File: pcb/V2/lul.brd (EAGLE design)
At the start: 90 x 96 mm, 85 parts, among them IC1 STM32F072C8T6, IC2 REG1117, IC3 74AHCT1G08DBV, SW1 324_SW324_SWITCH_FOOT_HOLE, SW10 KAILH_SWITCH_SOCKET, SW11 KAILH_SWITCH_SOCKET, SW12 KAILH_SWITCH_SOCKET, SW13 KAILH_SWITCH_SOCKET, SW14 KAILH_SWITCH_SOCKET, SW15 KAILH_SWITCH_SOCKET, SW16 KAILH_SWITCH_SOCKET, SW17 KAILH_SWITCH_SOCKET, SW18 KAILH_SWITCH_SOCKET, SW19 KAILH_SWITCH_SOCKET, SW2 324_SW324_SWITCH_FOOT_HOLE, SW3 324_SW324_SWITCH_FOOT_HOLE, SW4 324_SW324_SWITCH_FOOT_HOLE, SW5 KAILH_SWITCH_SOCKET, SW6 KAILH_SWITCH_SOCKET, SW7 KAILH_SWITCH_SOCKET, SW8 KAILH_SWITCH_SOCKET, SW9 KAILH_SWITCH_SOCKET, U1 UG-2864HSWEG01, U2 USBC_16P

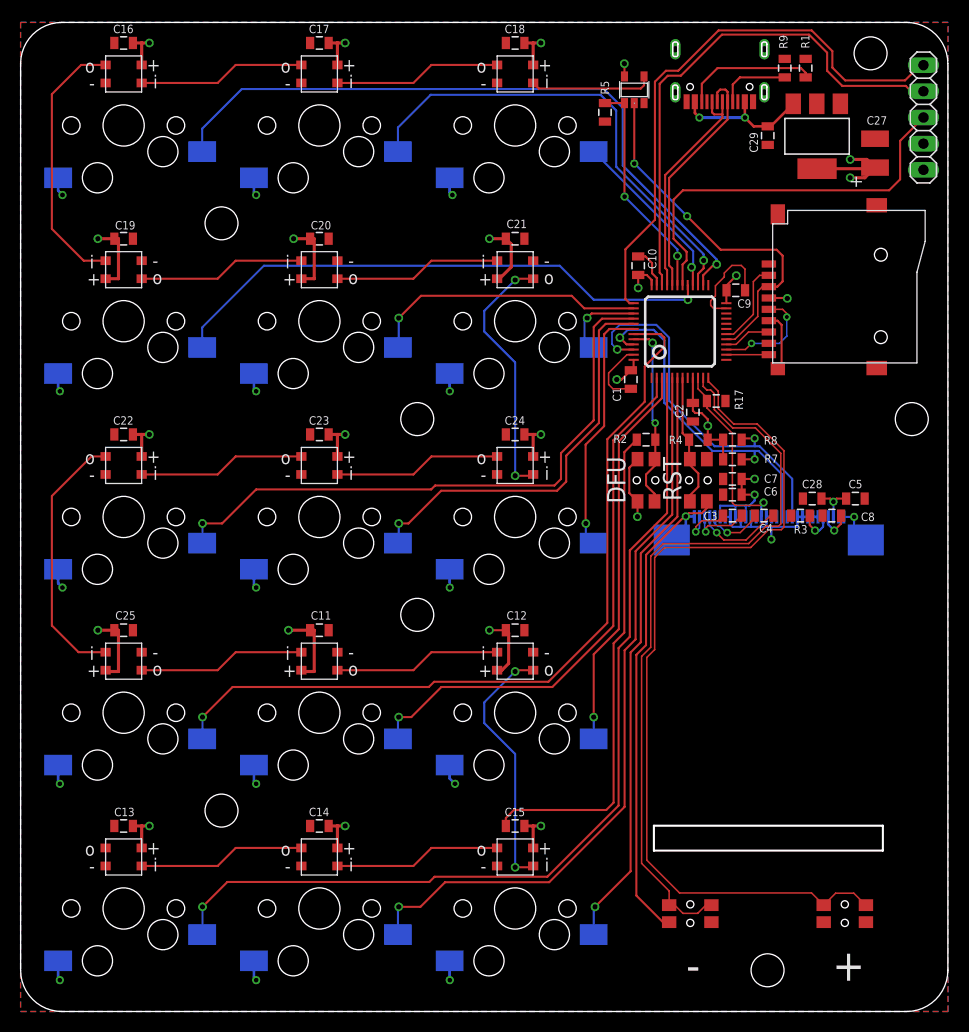
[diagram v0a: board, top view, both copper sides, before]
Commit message: added hot-swap sockets
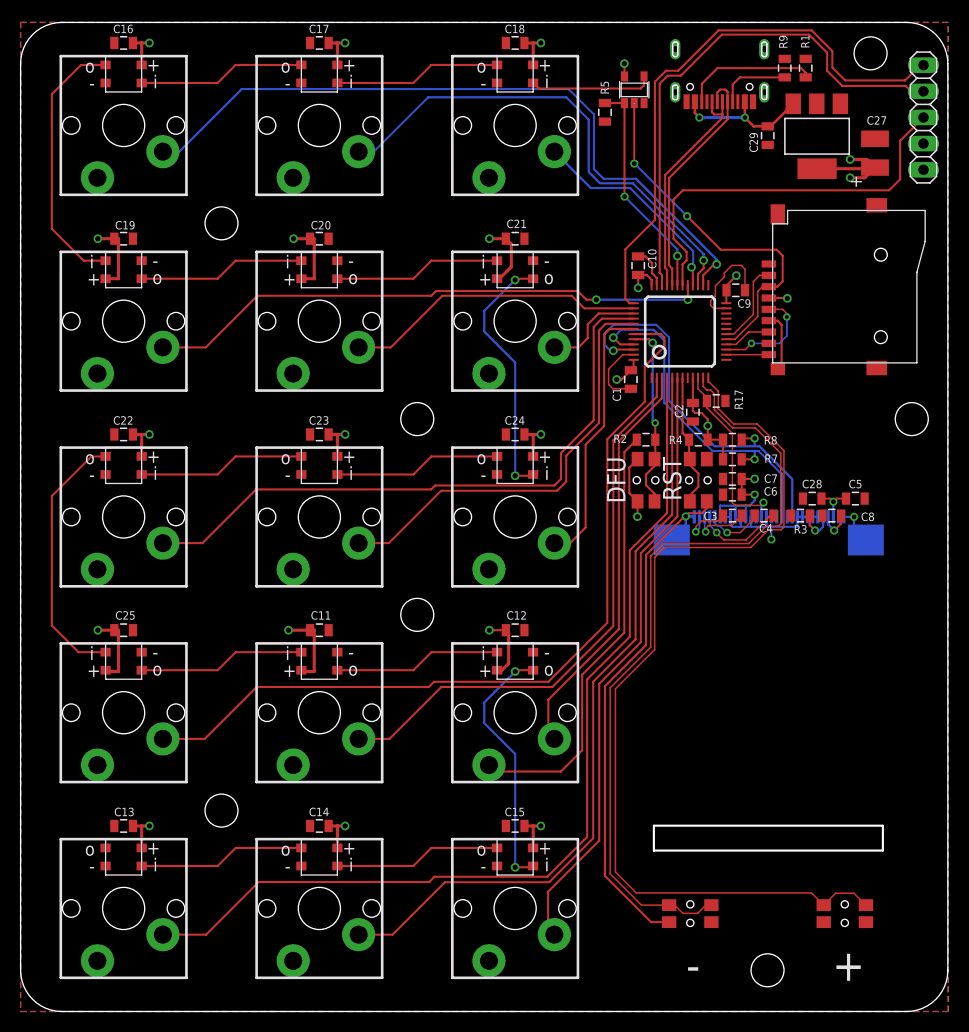
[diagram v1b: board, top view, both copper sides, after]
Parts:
- removed SW10, SW11, SW12, SW13, SW14, SW15, SW16, SW17, SW18, SW19, SW5, SW6, SW7, SW8, SW9: KAILH_SWITCH_SOCKET, Kailh_switch_socket:SWITCH_SOCKET
- added S1, S10, S11, S12, S13, S14, S15, S2, S3, S4, S5, S6, S7, S8, S9: CHERRY-MX-LED, SparkFun-Cherry-MX-Switch-Breakout:CHERRY-MX-LED
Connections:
- net GND: now also S1.S2, S10.S2, S11.S2, S12.S2, S13.S2, S14.S2, S15.S2, S2.S2, S3.S2, S4.S2, S5.S2, S6.S2, S7.S2, S8.S2, S9.S2; no longer SW10.1, SW11.1, SW12.1, SW13.1, SW14.1, SW15.1, SW16.1, SW17.1, SW18.1, SW19.1, SW5.1, SW6.1, SW7.1, SW8.1, SW9.1
- net SW1: now also S1.S1; no longer SW5.2
- net SW10: now also S10.S1; no longer SW14.2
- net SW11: now also S11.S1; no longer SW15.2
- net SW12: now also S12.S1; no longer SW16.2
- net SW13: now also S13.S1; no longer SW17.2
- net SW14: now also S14.S1; no longer SW18.2
- net SW15: now also S15.S1; no longer SW19.2
- net SW2: now also S2.S1; no longer SW6.2
- net SW3: now also S3.S1; no longer SW7.2
- net SW4: now also S4.S1; no longer SW8.2
- net SW5: now also S5.S1; no longer SW9.2
- net SW6: now also S6.S1; no longer SW10.2
- net SW7: now also S7.S1; no longer SW11.2
- net SW8: now also S8.S1; no longer SW12.2
- net SW9: now also S9.S1; no longer SW13.2
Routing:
- net GND: track 172.6 -> 142.6 mm, vias 18 -> 3
- net BUTTON2: track 86.4 -> 91.3 mm
- net BUTTON1: track 72.8 -> 76.9 mm
- net SW3: track 17.1 -> 20.9 mm
- net SW8: track 39.5 -> 42.2 mm, vias 1 -> 0
- net SW7: track 58.8 -> 61.5 mm, vias 1 -> 0
- net SW11: track 52.5 -> 55.1 mm, vias 1 -> 0
- net SW10: track 78.3 -> 80.9 mm, vias 1 -> 0
- net SW1: track 67.1 -> 69.4 mm
- net SW14: track 72.2 -> 74.5 mm, vias 1 -> 0
- net SW13: track 90.6 -> 92.9 mm, vias 1 -> 0
- net SW5: track 27.1 -> 29.3 mm, vias 1 -> 0
- net SW15: track 57.4 -> 59.5 mm, vias 1 -> 0
- net SW12: track 37.8 -> 39.8 mm, vias 1 -> 0
- net SW2: track 46.2 -> 48.2 mm
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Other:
- board text added: "dekuNukem PD1 JUN19"
- board text removed: "dekuNukem PD2 MAY20"
